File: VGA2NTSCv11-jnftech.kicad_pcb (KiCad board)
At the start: 2 copper layers, 58.4 x 99.8 mm, 57 parts, among them J1 RCA Jack Yellow, J3 DIN-4 S-Video Jack, J5 RCA Jack White, J6 RCA Jack Red, U2 RGB to Video Encoder, U3 Counter + Oscillator, X1 CRYSTAL 28.63636MHZ 18PF SMD

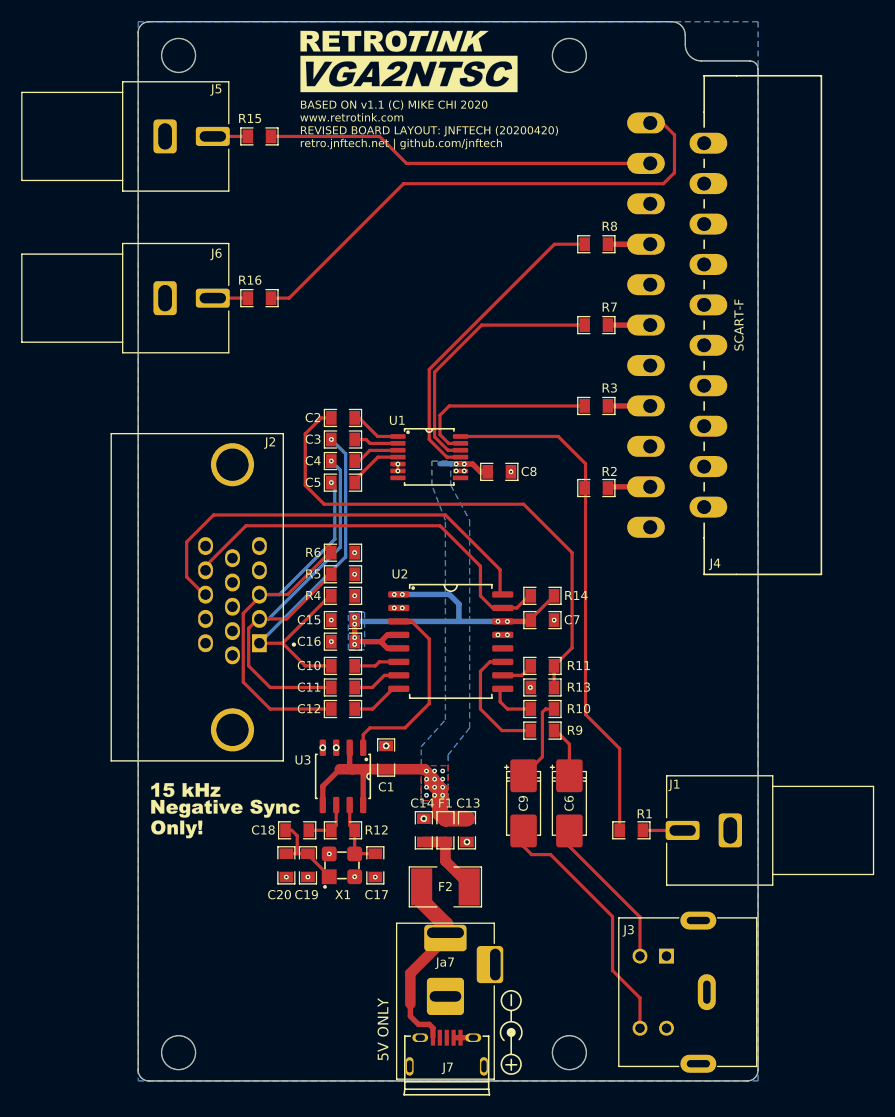
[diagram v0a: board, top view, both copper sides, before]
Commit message: Cleanup associations between schematic, PCB, and Netlist
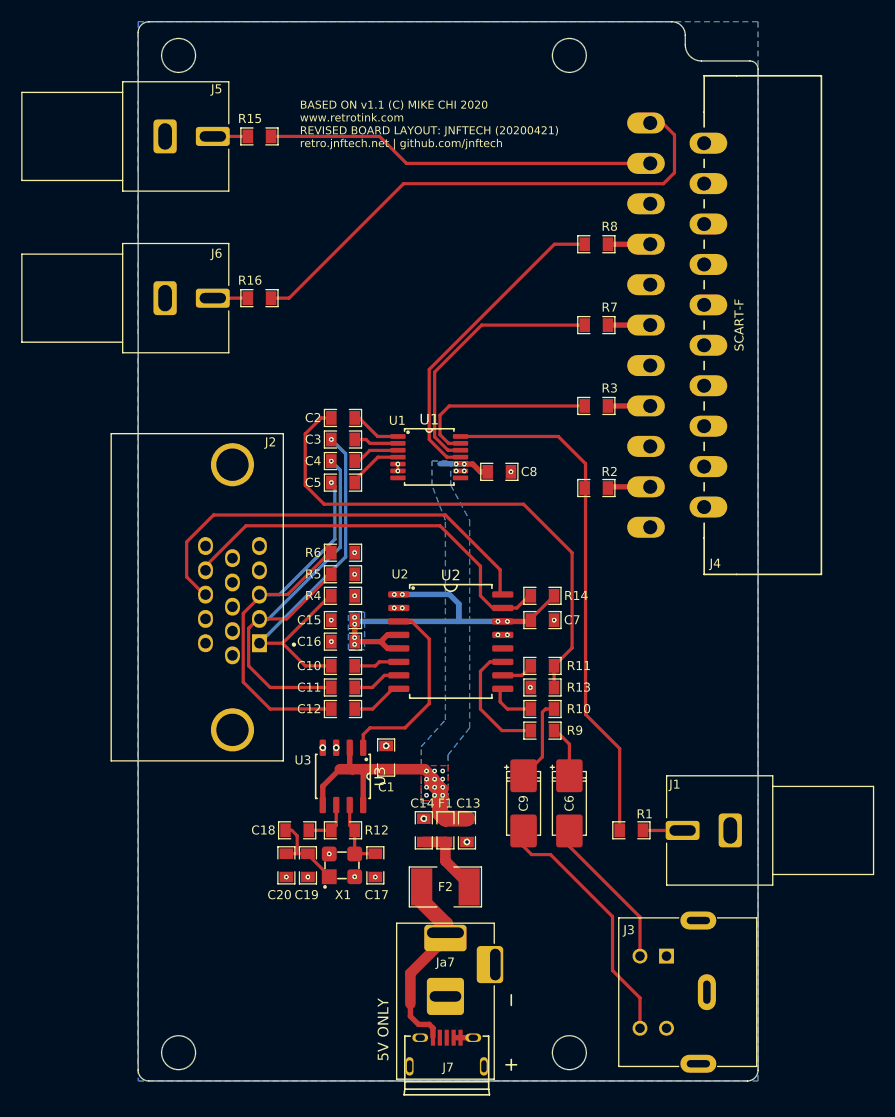
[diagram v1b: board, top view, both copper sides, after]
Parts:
- removed G***: LOGO, VGA2NTSC:Logo_RetroTink_VGA2NTSC
- removed G***: LOGO, VGA2NTSC:Logo_15khzNegativeSyncOnly
- removed the REF** at (164.8, 118.9)
- C1, C10, C11, C12, C16, C2, C3, C4, C5, C7, C8: value Capacitor -> 0.1uF
- C13, C14: value Capacitor -> Cap 10uF 0603
- C15: value Capacitor -> 10uF
- C17: value Capacitor -> 18pF
- C18, C19, C20: value Capacitor -> 47pF
- C6, C9: value Capacitor -> Cap 100uF 1210
- F1: value Ferrite Bead 220 Ohm 100Mhz 100mOhm DC -> Ferrite Bead
- F2: value PTC Fuse 500mA -> PTC 500mA
- J1: value RCA Jack Yellow -> RCA Yellow
- J2: value (none) -> ~
- J3: value DIN-4 S-Video Jack -> MD-40SM
- J4: value (none) -> SCART Female
- J5: value RCA Jack White -> RCA White
- J6: value RCA Jack Red -> RCA Red
- J7: value (none) -> Micro USB
- R1, R10, R2, R3, R4, R5, R6, R7, R8, R9: value Resistor 75 0402 -> 75
- R11, R13: value Resistor 1k 0402 -> Res 1k 0402
- R12: value Resistor 1M 0402 -> Res 1M 0402
- R14: value Resistor 4.7k 0402 -> 4.7k
- R15, R16: value Resistor 49.9 0402 -> 49.9
- U1: value (none) -> Video Buffer
- U2: value RGB to Video Encoder -> Encoder
- U3: value Counter + Oscillator -> OSC/DIV
- X1: value CRYSTAL 28.63636MHZ 18PF SMD -> XTAL
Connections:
- net BIN renamed /BIN
- net BOUT renamed /BOUT
- net CHROMA_OUT renamed /CHROMA_OUT
- net CLOCK renamed /CLOCK
- net CSYNC_OUT renamed /CSYNC_OUT
- net CVBS_OUT renamed /CVBS_OUT
- net GIN renamed /GIN
- net GOUT renamed /GOUT
- net HS renamed /HS
- net LUMA_OUT renamed /LUMA_OUT
- net NetC10_2 renamed Net-(C10-Pad2)
- net NetC11_2 renamed Net-(C11-Pad2)
- net NetC12_2 renamed Net-(C12-Pad2)
- net NetC14_1 renamed Net-(C14-Pad1)
- net NetC17_2 renamed Net-(C17-Pad2)
- net NetC18_1 renamed Net-(C18-Pad1)
- net NetC18_2 renamed Net-(C18-Pad2)
- net NetC2_1 renamed Net-(C2-Pad1)
- net NetC2_2 renamed Net-(C2-Pad2)
- net NetC3_2 renamed Net-(C3-Pad2)
- net NetC4_2 renamed Net-(C4-Pad2)
- net NetC5_2 renamed Net-(C5-Pad2)
- net NetC6_1 renamed Net-(C6-Pad1)
- net NetC9_1 renamed Net-(C9-Pad1)
- net NetF2_2 renamed Net-(F2-Pad2)
- net NetJ4_1 renamed Net-(J4-Pad1)
- net NetJ4_3 renamed Net-(J4-Pad3)
- net NetJ5_2B renamed Net-(J5-Pad2B)
- net NetJ6_2B renamed Net-(J6-Pad2B)
- net NetR10_1 renamed Net-(R10-Pad1)
- net NetR11_1 renamed Net-(R11-Pad1)
- net NetR1_1 renamed Net-(R1-Pad1)
- net NetR3_1 renamed Net-(R3-Pad1)
- net NetR7_1 renamed Net-(R7-Pad1)
- net NetR8_1 renamed Net-(R8-Pad1)
- net NetR9_1 renamed Net-(R9-Pad1)
- net RIN renamed /RIN
- net ROUT renamed /ROUT
- net VS renamed /VS
- J2 pad 11: (no net) -> Net-(J2-Pad11)
- J2 pad 12: (no net) -> Net-(J2-Pad12)
- J2 pad 15: (no net) -> Net-(J2-Pad15)
- J2 pad 4: (no net) -> Net-(J2-Pad4)
- J2 pad 9: (no net) -> Net-(J2-Pad9)
- J4 pad 10: (no net) -> Net-(J4-Pad10)
- J4 pad 12: (no net) -> Net-(J4-Pad12)
- J4 pad 14: (no net) -> Net-(J4-Pad14)
- J4 pad 16: (no net) -> Net-(J4-Pad16)
- J4 pad 2: (no net) -> Net-(J4-Pad2)
- J4 pad 20: (no net) -> Net-(J4-Pad20)
- J4 pad 6: (no net) -> Net-(J4-Pad6)
- J4 pad 8: (no net) -> Net-(J4-Pad8)
- J7 pad 2: (no net) -> Net-(J7-Pad2)
- J7 pad 3: (no net) -> Net-(J7-Pad3)
- Ja7 pad 3: (no net) -> Net-(Ja7-Pad3)
- U1 pad 7: (no net) -> Net-(U1-Pad7)
- U1 pad 8: (no net) -> Net-(U1-Pad8)
- U2 pad 12: (no net) -> Net-(U2-Pad12)
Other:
- board text added: "BASED ON v1.1 (C) MIKE CHI 2020 www.retrotink.com REVISED BOARD LAYOUT: JNFTECH (20200421) retro.jnftech.net | github.com/jnftech"
- board text removed: "BASED ON v1.1 (C) MIKE CHI 2020 www.retrotink.com REVISED BOARD LAYOUT: JNFTECH (20200420) retro.jnftech.net | github.com/jnftech"

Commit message: Add files via upload
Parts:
- added G***: LOGO, VGA2NTSC:Logo_15khzNegativeSyncOnly, F.Cu at (137.9, 97.8)
- added G***: LOGO, VGA2NTSC:Logo_RetroTink_VGA2NTSC, F.Cu at (155.2, 30.0)

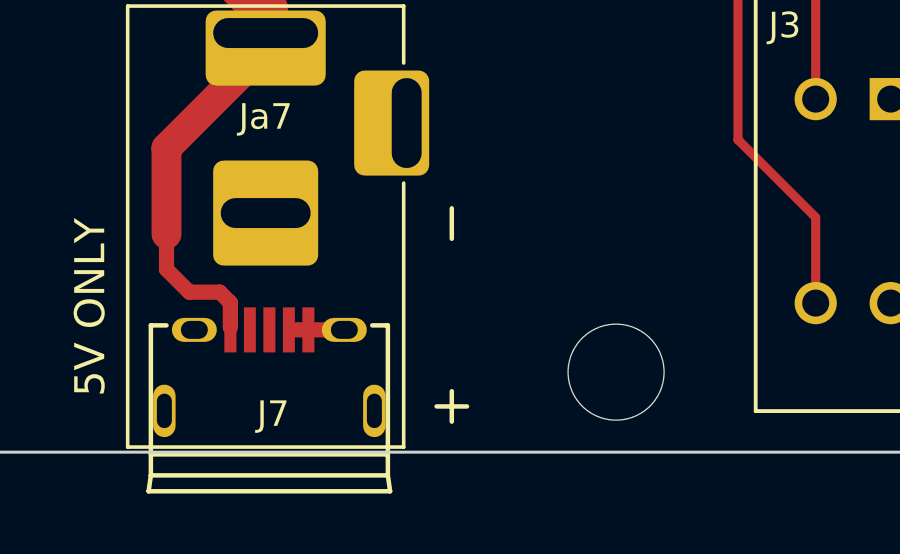
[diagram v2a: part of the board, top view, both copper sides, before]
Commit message: Fix Polarity silkscreen
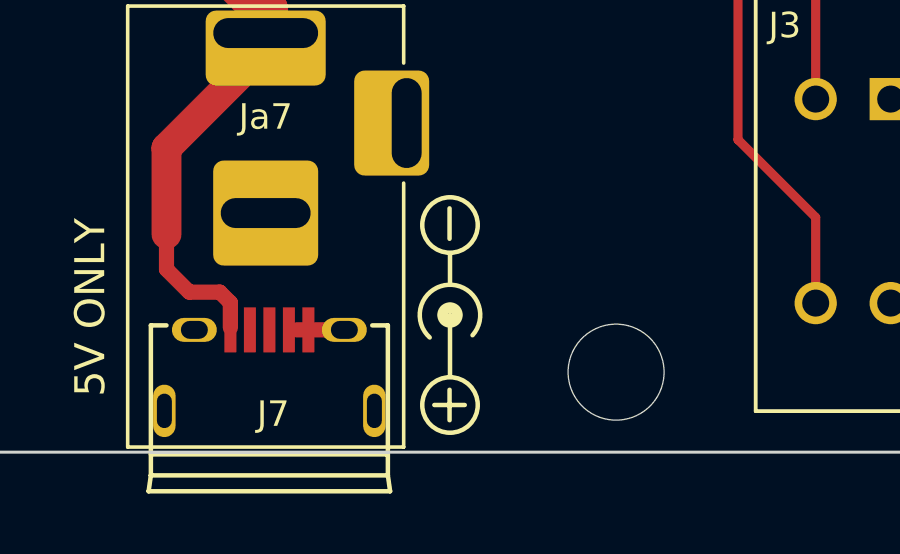
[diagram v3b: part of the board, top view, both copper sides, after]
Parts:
- added REF**: Symbol_Barrel_Polarity, Symbols:Symbol_Barrel_Polarity, F.Cu at (164.7, 118.9)
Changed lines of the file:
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@@
     (tracks 293)
     (zones 0)
-    (modules 56)
+    (modules 57)
     (nets 61)
   )
@@
     (uvia_drill 0.127)
   )
+  (module Symbols:Symbol_Barrel_Polarity locked (layer F.Cu)
+    (at 164.719 118.872 270)
+    (descr "Barrel connector polarity indicator")
+    (tags "barrel polarity")
+    (fp_text reference REF** (at 0 -2 90) (layer F.SilkS) hide
+      (effects (font (size 1 1) (thickness 0.15)))
+    )
+    (fp_text value Symbol_Barrel_Polarity (at 0 2 90) (layer F.Fab)
+      (effects (font (size 1 1) (thickness 0.15)))
+    )
+    (fp_line (start 0 0.075) (end 2 0.075) (layer F.SilkS) (width 0.15))
+    (fp_line (start -2 0.075) (end -1.1 0.075) (layer F.SilkS) (width 0.15))
+    (fp_circle (center -3 0.075) (end -3 1) (layer F.SilkS) (width 0.15))
+    (fp_circle (center 3 0.075) (end 3 1) (layer F.SilkS) (width 0.15))
+    (fp_circle (center 0 0.075) (end 0 0.25) (layer F.SilkS) (width 0.5))
+    (fp_arc (start 0 0.075) (end 0.75 0.75) (angle 270) (layer F.SilkS) (width 0.15))
+  )
   (module VGA2NTSC:Logo_15khzNegativeSyncOnly locked (layer F.Cu)
     (at 137.922 97.79)
@@
     (effects (font (size 1 1) (thickness 0.15)))
   )
-  (gr_line (start 164.704 116.332) (end 164.704 115.316) (layer F.SilkS) (width 0.15))
-  (gr_line (start 164.704 121.412) (end 164.704 122.428) (layer F.SilkS) (width 0.15))
-  (gr_line (start 164.196 121.92) (end 165.212 121.92) (layer F.SilkS) (width 0.15))
+  (gr_line (start 164.629 116.332) (end 164.629 115.316) (layer F.SilkS) (width 0.15))
+  (gr_line (start 164.629 121.364) (end 164.629 122.38) (layer F.SilkS) (width 0.15))
+  (gr_line (start 164.121 121.872) (end 165.137 121.872) (layer F.SilkS) (width 0.15))
   (gr_text "BASED ON v1.1 (C) MIKE CHI 2020\nwww.retrotink.com\nREVISED BOARD LAYOUT: JNFTECH (20200421)\nretro.jnftech.net | github.com/jnftech" (at 144.78 33.274) (layer F.SilkS)
     (effects (font (size 0.75 0.75) (thickness 0.15)) (justify left))

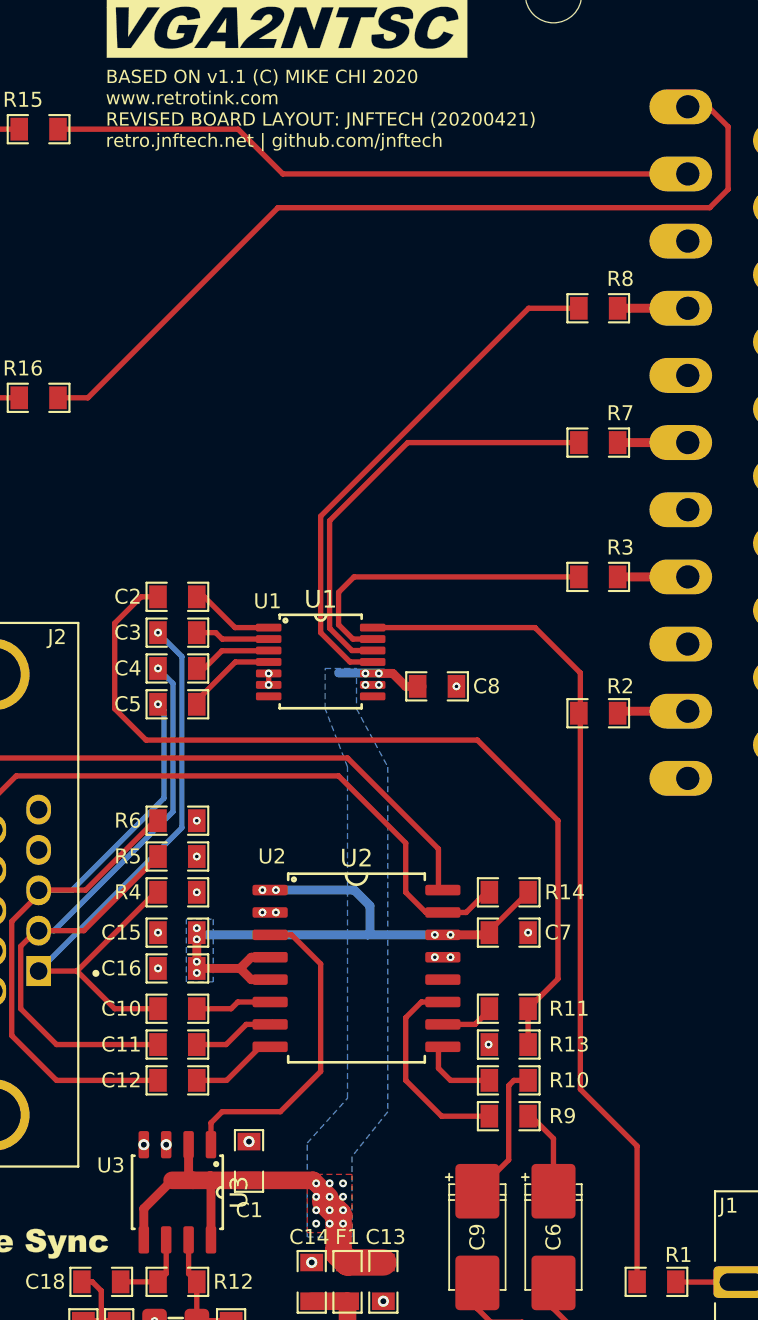
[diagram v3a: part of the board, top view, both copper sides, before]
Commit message: Fix silkscreen errors
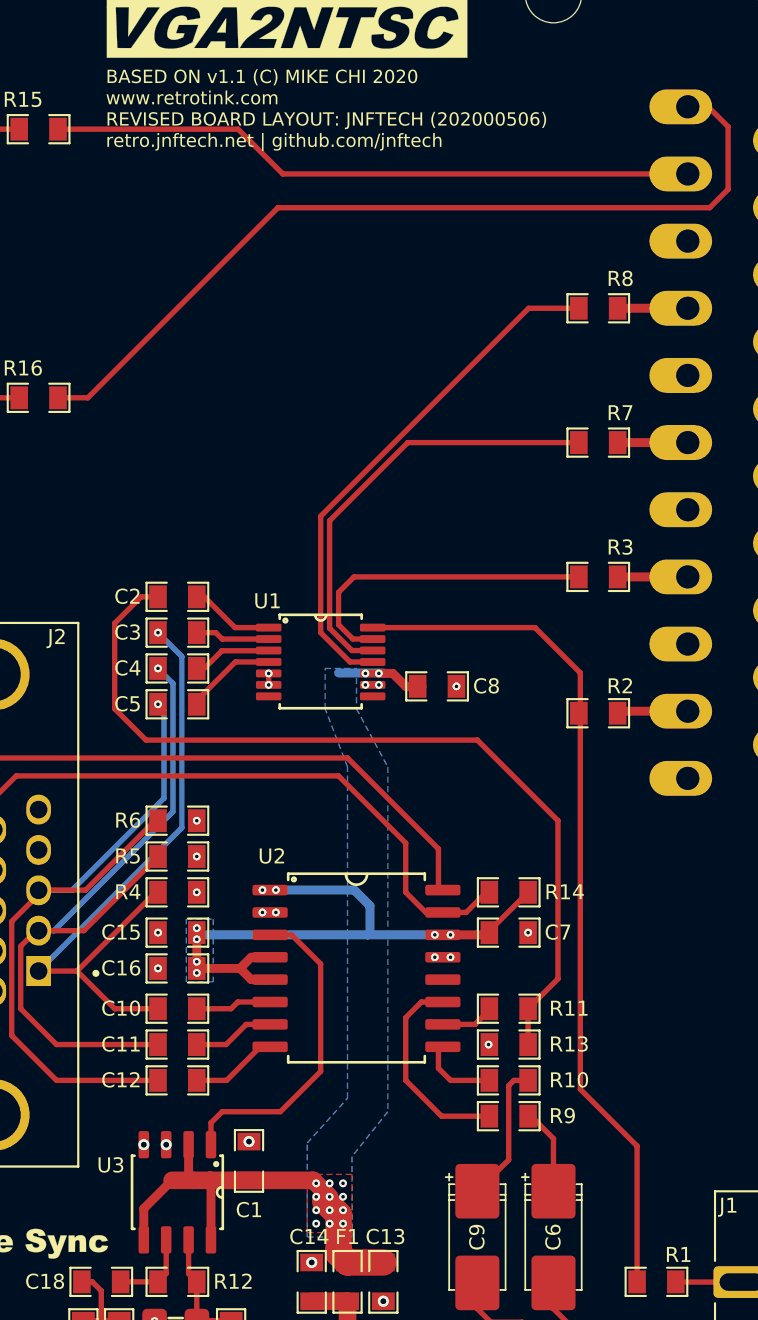
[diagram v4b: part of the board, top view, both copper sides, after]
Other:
- board text added: "BASED ON v1.1 (C) MIKE CHI 2020 www.retrotink.com REVISED BOARD LAYOUT: JNFTECH (202000506) retro.jnftech.net | github.com/jnftech"
- board text removed: "BASED ON v1.1 (C) MIKE CHI 2020 www.retrotink.com REVISED BOARD LAYOUT: JNFTECH (20200421) retro.jnftech.net | github.com/jnftech"
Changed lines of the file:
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@@
     (tags "SSOP 0.65")
     (attr smd)
-    (fp_text reference U1 (at 0 -3.55) (layer F.SilkS)
+    (fp_text reference U1 (at 0 0.114) (layer F.SilkS) hide
       (effects (font (size 1 1) (thickness 0.15)))
     )
@@
     (tags "SOIC 1.27")
     (attr smd)
-    (fp_text reference U2 (at 0 -6.25) (layer F.SilkS)
+    (fp_text reference U2 (at 0 0) (layer F.SilkS) hide
       (effects (font (size 1 1) (thickness 0.15)))
     )
@@
     (tags "SOIC 1.27")
     (attr smd)
-    (fp_text reference U3 (at 0 -3.5 90) (layer F.SilkS)
+    (fp_text reference U3 (at 0 0 90) (layer F.SilkS) hide
       (effects (font (size 1 1) (thickness 0.15)))
     )
@@
   (gr_line (start 164.629 121.364) (end 164.629 122.38) (layer F.SilkS) (width 0.15))
   (gr_line (start 164.121 121.872) (end 165.137 121.872) (layer F.SilkS) (width 0.15))
-  (gr_text "BASED ON v1.1 (C) MIKE CHI 2020\nwww.retrotink.com\nREVISED BOARD LAYOUT: JNFTECH (20200421)\nretro.jnftech.net | github.com/jnftech" (at 144.78 33.274) (layer F.SilkS)
+  (gr_text "BASED ON v1.1 (C) MIKE CHI 2020\nwww.retrotink.com\nREVISED BOARD LAYOUT: JNFTECH (202000506)\nretro.jnftech.net | github.com/jnftech" (at 144.78 33.274) (layer F.SilkS)
     (effects (font (size 0.75 0.75) (thickness 0.15)) (justify left))
   )
